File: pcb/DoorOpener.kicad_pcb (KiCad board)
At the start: 2 copper layers, 27.7 x 36.4 mm, 7 parts, among them J1 Serial, SW1 POWER, SW2 Button, U2 ESP-01v090

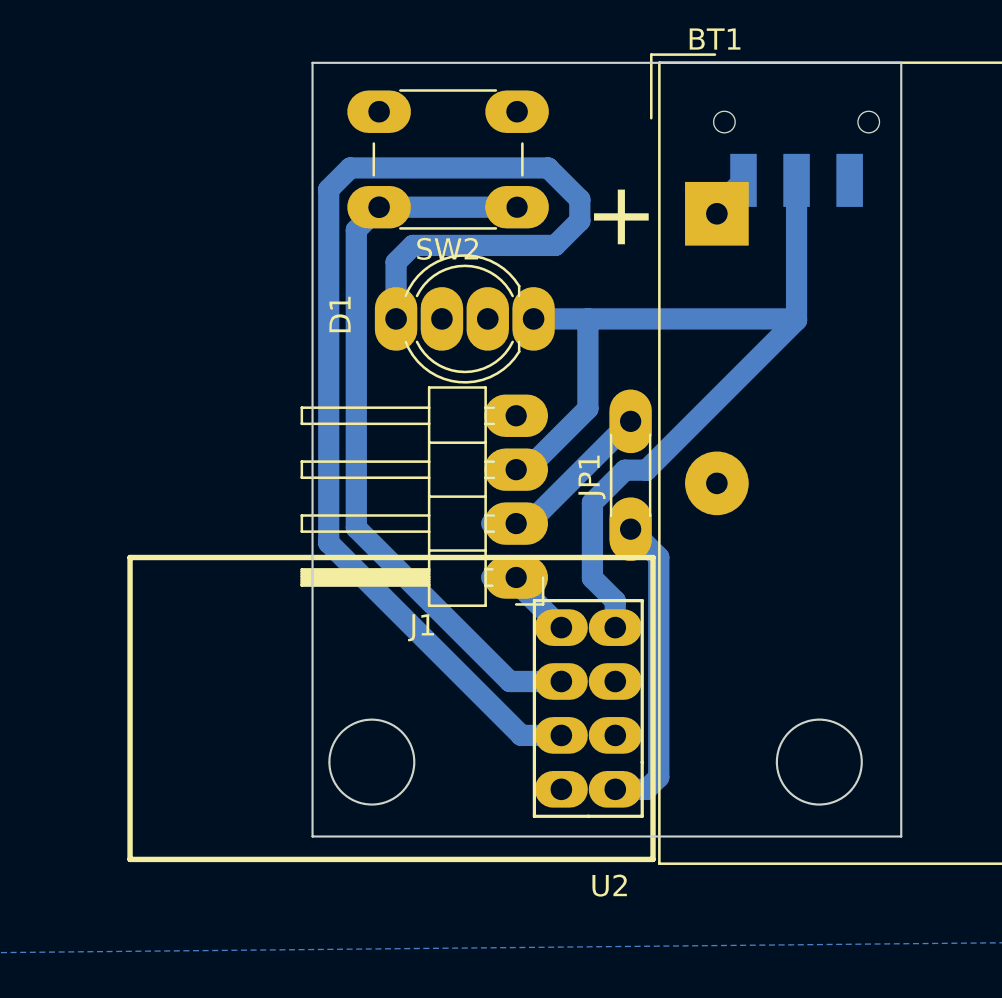
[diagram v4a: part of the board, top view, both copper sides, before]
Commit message: Make the pads as big as possible
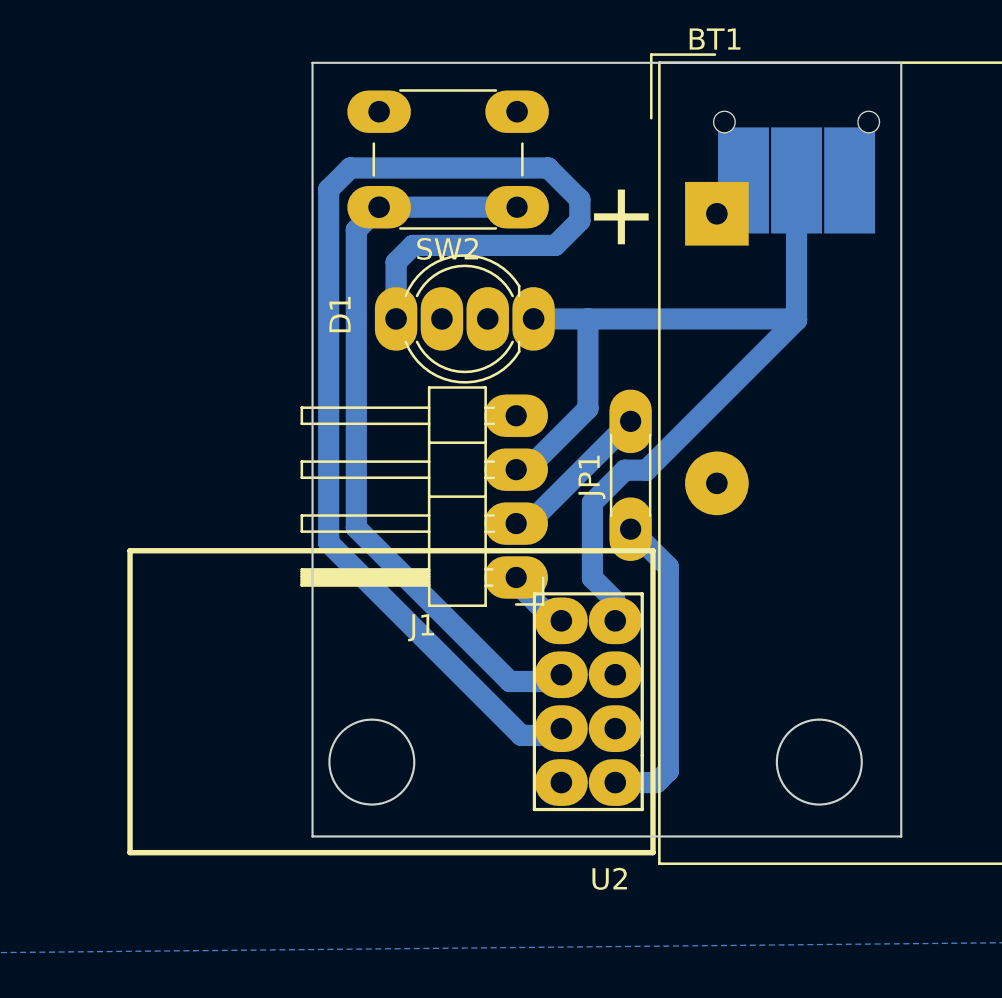
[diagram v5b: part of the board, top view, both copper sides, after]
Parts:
- moved U2 0.32 mm to (87.7, 156.5)
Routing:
- net Net-(J1-Pad2): track 8.54 -> 6.81 mm
- net /RX: track 4.26 -> 3.34 mm
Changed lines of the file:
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@@
     (pad_to_mask_clearance 0)
     (pcbplotparams
-      (layerselection 0x0001020_7fffffff)
+      (layerselection 0x0001010_7fffffff)
       (disableapertmacros false)
       (usegerberextensions false)
@@
       (drillshape 0)
       (scaleselection 1)
-      (outputdirectory "plot")
+      (outputdirectory "plot-0.2")
     )
   )
@@
   )
   (footprint "ESP8266:ESP-01" (layer "F.Cu")
-    (at 87.668318 156.782594 180)
+    (at 87.668318 156.464 180)
     (descr "Module, ESP-8266, ESP-01, 8 pin")
     (tags "Module ESP-8266 ESP8266")
@@
     (fp_line (start -1.778 10.922) (end -1.778 -3.302) (layer "F.Fab") (width 0.05))
     (fp_line (start 22.86 10.922) (end -1.778 10.922) (layer "F.Fab") (width 0.05))
-    (pad "1" thru_hole oval (at 0 0 180) (size 2.5 1.7272) (drill 1.016) (layers *.Cu *.Mask "F.SilkS")
+    (pad "1" thru_hole oval (at 0 0 180) (size 2.5 2.2) (drill 1.016) (layers *.Cu *.Mask "F.SilkS")
       (net 3 "/TX") (pinfunction "UTXD") (pintype "output"))
-    (pad "2" thru_hole oval (at 2.54 0 180) (size 2.5 1.7272) (drill 1.016) (layers *.Cu *.Mask "F.SilkS")
+    (pad "2" thru_hole oval (at 2.54 0 180) (size 2.5 2.2) (drill 1.016) (layers *.Cu *.Mask "F.SilkS")
       (net 6 "GND") (pinfunction "GND") (pintype "power_in"))
-    (pad "3" thru_hole oval (at 0 2.54 180) (size 2.5 1.7272) (drill 1.016) (layers *.Cu *.Mask "F.SilkS")
+    (pad "3" thru_hole oval (at 0 2.54 180) (size 2.5 2.2) (drill 1.016) (layers *.Cu *.Mask "F.SilkS")
       (net 1 "unconnected-(U2-Pad3)") (pinfunction "CH_PD") (pintype "input+no_connect"))
-    (pad "4" thru_hole oval (at 2.54 2.54 180) (size 2.5 1.7272) (drill 1.016) (layers *.Cu *.Mask "F.SilkS")
+    (pad "4" thru_hole oval (at 2.54 2.54 180) (size 2.5 2.2) (drill 1.016) (layers *.Cu *.Mask "F.SilkS")
       (net 8 "Net-(D1-Pad4)") (pinfunction "GPIO2") (pintype "tri_state"))
-    (pad "5" thru_hole oval (at 0 5.08 180) (size 2.5 1.7272) (drill 1.016) (layers *.Cu *.Mask "F.SilkS")
+    (pad "5" thru_hole oval (at 0 5.08 180) (size 2.5 2.2) (drill 1.016) (layers *.Cu *.Mask "F.SilkS")
       (net 2 "unconnected-(U2-Pad5)") (pinfunction "RST") (pintype "input+no_connect"))
-    (pad "6" thru_hole oval (at 2.54 5.08 180) (size 2.5 1.7272) (drill 1.016) (layers *.Cu *.Mask "F.SilkS")
+    (pad "6" thru_hole oval (at 2.54 5.08 180) (size 2.5 2.2) (drill 1.016) (layers *.Cu *.Mask "F.SilkS")
       (net 10 "Net-(SW2-Pad1)") (pinfunction "GPIO0") (pintype "tri_state"))
-    (pad "7" thru_hole oval (at 0 7.62 180) (size 2.5 1.7272) (drill 1.016) (layers *.Cu *.Mask "F.SilkS")
+    (pad "7" thru_hole oval (at 0 7.62 180) (size 2.5 2.2) (drill 1.016) (layers *.Cu *.Mask "F.SilkS")
       (net 7 "+3V3") (pinfunction "VCC") (pintype "power_in"))
-    (pad "8" thru_hole oval (at 2.54 7.62 180) (size 2.5 1.7272) (drill 1.016) (layers *.Cu *.Mask "F.SilkS")
+    (pad "8" thru_hole oval (at 2.54 7.62 180) (size 2.5 2.2) (drill 1.016) (layers *.Cu *.Mask "F.SilkS")
       (net 9 "/RX") (pinfunction "URXD") (pintype "input"))
     (model "${KIPRJMOD}/lib/esp8266/ESP8266.3dshapes/esp01.step"
@@
     (pad "" np_thru_hole circle (at -3.4 0) (size 0.9 0.9) (drill 1.016) (layers F&B.Cu *.Mask))
     (pad "" np_thru_hole circle (at 3.4 0) (size 0.9 0.9) (drill 1.016) (layers F&B.Cu *.Mask))
-    (pad "1" smd rect (at -2.5 2.75) (size 1.25 2.5) (layers "B.Cu" "B.Paste" "B.Mask")
+    (pad "1" smd rect (at -2.5 2.75) (size 2.4 5) (layers "B.Cu" "B.Paste" "B.Mask")
       (net 5 "Net-(BT1-Pad1)") (pinfunction "A") (pintype "passive"))
-    (pad "2" smd rect (at 0 2.75) (size 1.25 2.5) (layers "B.Cu" "B.Paste" "B.Mask")
+    (pad "2" smd rect (at 0 2.75) (size 2.4 5) (layers "B.Cu" "B.Paste" "B.Mask")
       (net 7 "+3V3") (pinfunction "B") (pintype "passive"))
-    (pad "3" smd rect (at 2.5 2.75) (size 1.25 2.5) (layers "B.Cu" "B.Paste" "B.Mask"))
+    (pad "3" smd rect (at 2.5 2.75) (size 2.4 5) (layers "B.Cu" "B.Paste" "B.Mask"))
     (model "${KICAD6_3DMODEL_DIR}/Button_Switch_SMD.3dshapes/SW_SPDT_CK-JS102011SAQN.wrl"
       (offset (xyz 0 0 0))
@@
     (effects (font (size 1.5 1.5) (thickness 0.25)))
   )
-  (segment (start 87.668318 156.782594) (end 89.145518 156.782594) (width 1) (layer "B.Cu") (net 3))
-  (segment (start 89.718318 156.209794) (end 89.718318 145.852318) (width 1) (layer "B.Cu") (net 3))
-  (segment (start 89.145518 156.782594) (end 89.718318 156.209794) (width 1) (layer "B.Cu") (net 3))
-  (segment (start 89.718318 145.852318) (end 88.392 144.526) (width 1) (layer "B.Cu") (net 3))
+  (segment (start 90.17 146.304) (end 88.392 144.526) (width 1) (layer "B.Cu") (net 3))
+  (segment (start 89.618318 156.464) (end 90.17 155.912318) (width 1) (layer "B.Cu") (net 3))
+  (segment (start 90.17 155.912318) (end 90.17 146.304) (width 1) (layer "B.Cu") (net 3))
+  (segment (start 87.668318 156.464) (end 89.618318 156.464) (width 1) (layer "B.Cu") (net 3))
   (segment (start 92.456 129.3488) (end 93.71 128.0948) (width 1) (layer "B.Cu") (net 5))
   (segment (start 92.456 129.667) (end 92.456 129.3488) (width 1) (layer "B.Cu") (net 5))
@@
   (segment (start 86 130) (end 86 129) (width 1) (layer "B.Cu") (net 8))
   (segment (start 84.508 127.508) (end 75.184 127.508) (width 1) (layer "B.Cu") (net 8))
-  (segment (start 81.845 146.802) (end 82.767724 146.802) (width 1) (layer "B.Cu") (net 9))
   (segment (start 82.767724 146.802) (end 85.128318 149.162594) (width 1) (layer "B.Cu") (net 9))
   (segment (start 75.467501 130.432894) (end 75.467501 144.467501) (width 1) (layer "B.Cu") (net 10))
@@
   (segment (start 82.702594 151.702594) (end 85.128318 151.702594) (width 1) (layer "B.Cu") (net 10))
   (segment (start 83.576 144.262) (end 88.392 139.446) (width 1) (layer "B.Cu") (net 11))
-  (segment (start 81.845 144.262) (end 83.576 144.262) (width 1) (layer "B.Cu") (net 11))
   (zone (net 6) (net_name "GND") (layer "B.Cu") (hatch edge 0.508)
     (connect_pads (clearance 0.508))

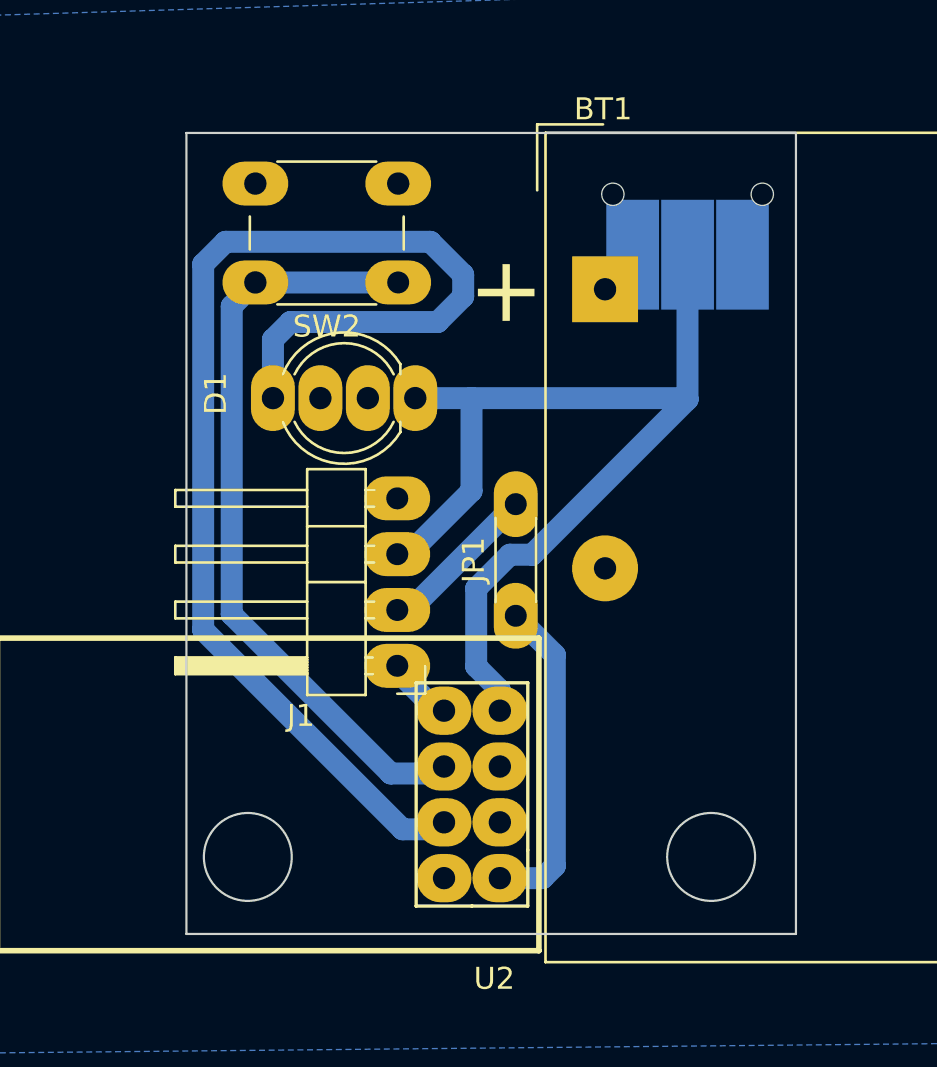
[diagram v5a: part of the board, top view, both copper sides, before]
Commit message: Add FTDI-compatible socket and an option to power from USB
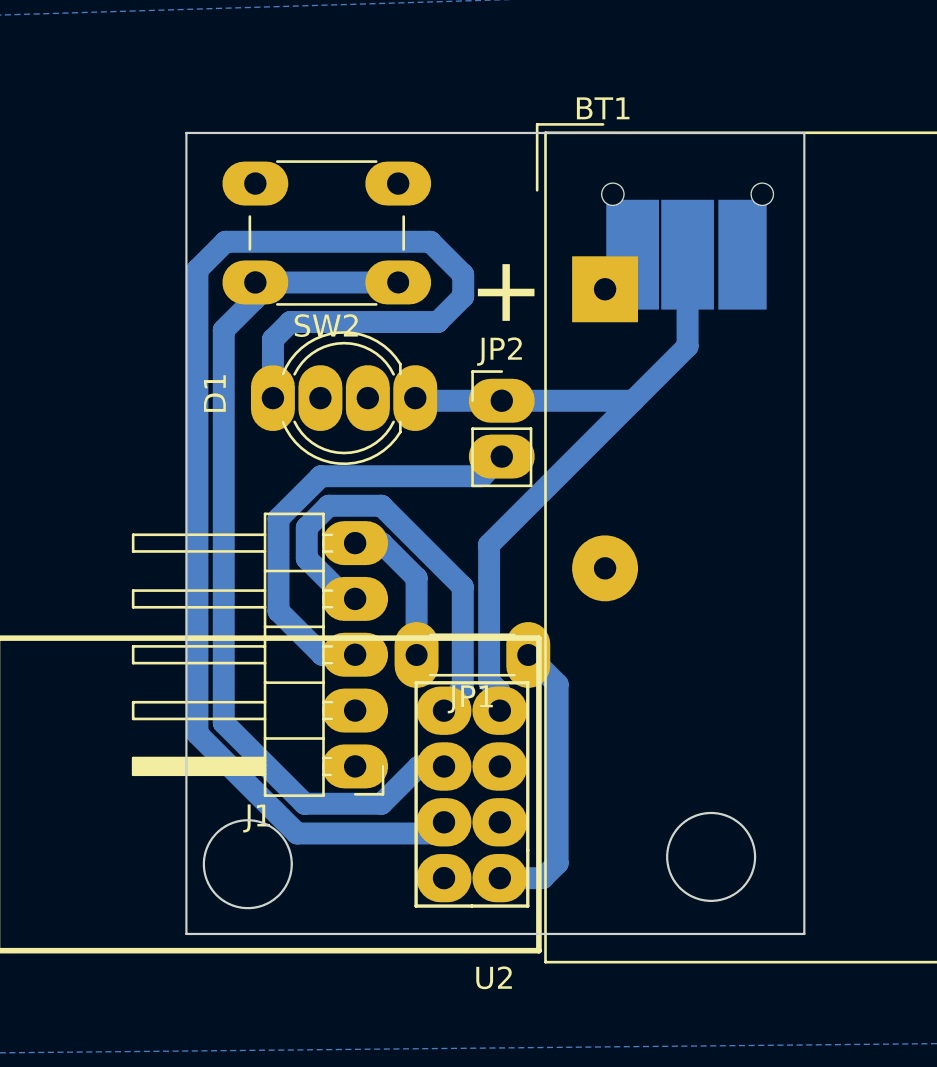
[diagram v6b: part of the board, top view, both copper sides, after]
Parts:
- added JP2: FTDI_Voltage, Connector_PinHeader_2.54mm:PinHeader_1x02_P2.54mm_Vertical, F.Cu at (87.8, 134.7)
- J1: footprint Connector_PinHeader_2.54mm:PinHeader_1x04_P2.54mm_Horizontal -> Connector_PinHeader_2.54mm:PinHeader_1x05_P2.54mm_Horizontal
- moved J1 4.96 mm to (81.1, 151.4)
- moved JP1 1.87 mm to (89.0, 146.3), turned to 180 degrees
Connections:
- J1 pad 1: /RX -> GND
- J1 pad 2: Net-(J1-Pad2) -> unconnected-(J1-Pad2)
- J1 pad 3: +3V3 -> Net-(J1-Pad3)
- J1 pad 4: GND -> /RX
- JP1 pad 2: Net-(J1-Pad2) -> Net-(JP1-Pad2)
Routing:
- net Net-(J1-Pad3): track 0.00 -> 19.8 mm
- net /RX: track 3.34 -> 20.0 mm
- net +3V3: track 47.3 -> 34.7 mm
- net Net-(JP1-Pad2): track 0.00 -> 6.96 mm
- net Net-(J1-Pad2): track 6.81 -> 0.00 mm
- net Net-(SW2-Pad1): track 34.7 -> 39.4 mm
- net Net-(D1-Pad4): track 57.4 -> 60.8 mm
- net /TX: track 14.9 -> 12.9 mm
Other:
- board size 27.7 x 36.4 mm -> 28.1 x 36.4 mm

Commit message: PCB: Add station module
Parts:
- added J2: Serial, Connector_PinHeader_2.54mm:PinHeader_1x05_P2.54mm_Horizontal, F.Cu at (158.5, 43.7)
- added J3: 14V, TerminalBlock_Phoenix:TerminalBlock_Phoenix_MPT-0,5-2-2.54_1x02_P2.54mm_Horizontal, F.Cu at (157.2, 87.4)
- added JP4: Voltage Source, Connector_PinHeader_2.54mm:PinHeader_1x03_P2.54mm_Vertical, F.Cu at (163.5, 47.9)
- added JP5: Bridge, Resistor_THT:R_Axial_DIN0204_L3.6mm_D1.6mm_P5.08mm_Horizontal, F.Cu at (173.6, 56.5)
- added JP6: Bridge, Resistor_THT:R_Axial_DIN0204_L3.6mm_D1.6mm_P5.08mm_Horizontal, F.Cu at (181.5, 46.9)
- added JP7: Bridge, Resistor_THT:R_Axial_DIN0204_L3.6mm_D1.6mm_P5.08mm_Horizontal, F.Cu at (176.6, 46.1)
- added SW4: Button, Button_Switch_THT:SW_PUSH_6mm_H4.3mm, F.Cu at (187.3, 48.9)
- added SW5: Reset, Button_Switch_THT:SW_PUSH_6mm_H4.3mm, F.Cu at (187.3, 60.7)
- added U2: ESP-01v090, ESP8266:ESP-01, F.Cu at (174.0, 52.6)
- added U3: dcdc, dcdc:dcdc, F.Cu at (159.8, 68.3)
- added U4: Relay, relais_module:relais_module, F.Cu at (180.7, 78.0)
- moved SW2 178.2 mm to (235.8, 37.6), turned to 90 degrees
- moved J1 176.1 mm to (213.7, 35.6), turned to 90 degrees
- moved D1 175.5 mm to (230.5, 38.4), turned to 90 degrees
- moved JP2 170.0 mm to (230.4, 42.3), turned to -90 degrees
- moved U1 166.4 mm to (208.7, 42.2), turned to 90 degrees
- moved JP1 165.6 mm to (218.8, 43.5), turned to 90 degrees
- moved BT1 165.2 mm to (235.5, 47.0), turned to -90 degrees
- moved SW1 161.8 mm to (239.8, 50.7), turned to -90 degrees
- renumbered U2 to U1
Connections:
- net Net-(BT1-Pad1) renamed /RAW_3V3
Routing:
- net (no net): track 0.00 -> 134.6 mm
- net +3V3: track 34.7 -> 93.3 mm
- net /TX: track 12.9 -> 16.9 mm
- net /RX: track 20.0 -> 23.9 mm
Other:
- board size 28.1 x 36.4 mm -> 90.9 x 68.1 mm
- board text added: "5(+) (-)3"
- board text added: "Make this modular"
- board text added: "REMOTE"
- board text added: "STATION"
- board text added: "shorten 5 and 6"
